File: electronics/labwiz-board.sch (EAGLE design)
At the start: 91 parts, among them J1 SD_MICRO_SDIO_1BIT, J2 CORTEX_DEBUGSMD, J3 DNP, U1 STM32F10XRXT6, U2 MCP73831, U4 MIC5219-3.3V, X2 M12_BOTTOM_CONTACTS_FPC_1MM, Y3 32.768kHz

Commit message: Updated .gitignore. Comitting unknown schematic updates.
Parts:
- removed J4: (no value), SparkFun-Connectors:M03PTH
- added TP10, TP8, TP9: DNP, PaxInstruments-Connectors:M01_PAD_1MM
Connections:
- net GND: now also TP10.P$1; no longer J4.3
- net USART1_RX: now also TP9.P$1; no longer J4.2
- net USART1_TX: now also TP8.P$1; no longer J4.1
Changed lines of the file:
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@@
 <part name="C16" library="PaxInstruments-RCL" deviceset="CAPACITOR_FIXED" device="_0402" technology="_100NF" value="100nF"/>
 <part name="TP7" library="PaxInstruments-Connectors" deviceset="M01" device="_PAD_1MM" value="DNP"/>
-<part name="J4" library="SparkFun-Connectors" deviceset="M03" device="PTH"/>
 <part name="GND21" library="PaxInstruments-Aesthetics" deviceset="GND" device="" value="GND"/>
+<part name="TP8" library="PaxInstruments-Connectors" deviceset="M01" device="_PAD_1MM" value="DNP"/>
+<part name="TP9" library="PaxInstruments-Connectors" deviceset="M01" device="_PAD_1MM" value="DNP"/>
+<part name="TP10" library="PaxInstruments-Connectors" deviceset="M01" device="_PAD_1MM" value="DNP"/>
 </parts>
 <sheets>
@@
 <instance part="C16" gate="G$1" x="165.1" y="63.5" rot="MR180"/>
 <instance part="TP7" gate="G$1" x="299.72" y="119.38" rot="R180"/>
-<instance part="J4" gate="J$1" x="281.94" y="121.92" rot="R180"/>
 <instance part="GND21" gate="G$1" x="271.78" y="116.84"/>
+<instance part="TP8" gate="G$1" x="276.86" y="124.46"/>
+<instance part="TP9" gate="G$1" x="276.86" y="121.92"/>
+<instance part="TP10" gate="G$1" x="276.86" y="119.38"/>
 </instances>
 <busses>
@@
 </segment>
 <segment>
-<pinref part="J4" gate="J$1" pin="3"/>
 <pinref part="GND21" gate="G$1" pin="GND"/>
 <wire x1="274.32" y1="119.38" x2="271.78" y2="119.38" width="0.1524" layer="91"/>
 <wire x1="271.78" y1="119.38" x2="271.78" y2="116.84" width="0.1524" layer="91"/>
+<pinref part="TP10" gate="G$1" pin="P$1"/>
 </segment>
 </net>
@@
 <segment>
 <label x="259.08" y="124.46" size="1.27" layer="95" rot="R180" xref="yes"/>
-<pinref part="J4" gate="J$1" pin="1"/>
 <wire x1="259.08" y1="124.46" x2="274.32" y2="124.46" width="0.1524" layer="91"/>
+<pinref part="TP8" gate="G$1" pin="P$1"/>
 </segment>
 <segment>
@@
 <segment>
 <label x="259.08" y="121.92" size="1.27" layer="95" rot="R180" xref="yes"/>
-<pinref part="J4" gate="J$1" pin="2"/>
 <wire x1="259.08" y1="121.92" x2="274.32" y2="121.92" width="0.1524" layer="91"/>
-</segment>
-<segment>
+<pinref part="TP9" gate="G$1" pin="P$1"/>
+</segment>
+<segment>

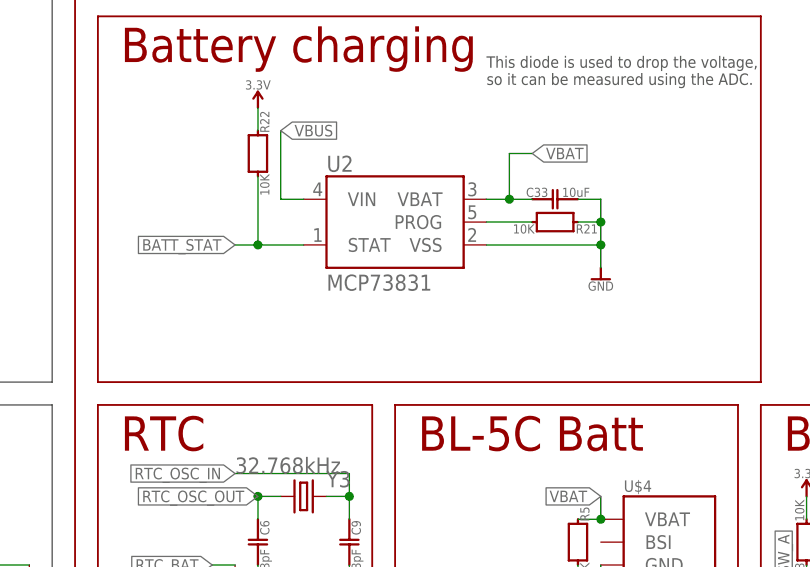
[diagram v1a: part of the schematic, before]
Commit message: Updated MCP73831/2 name.
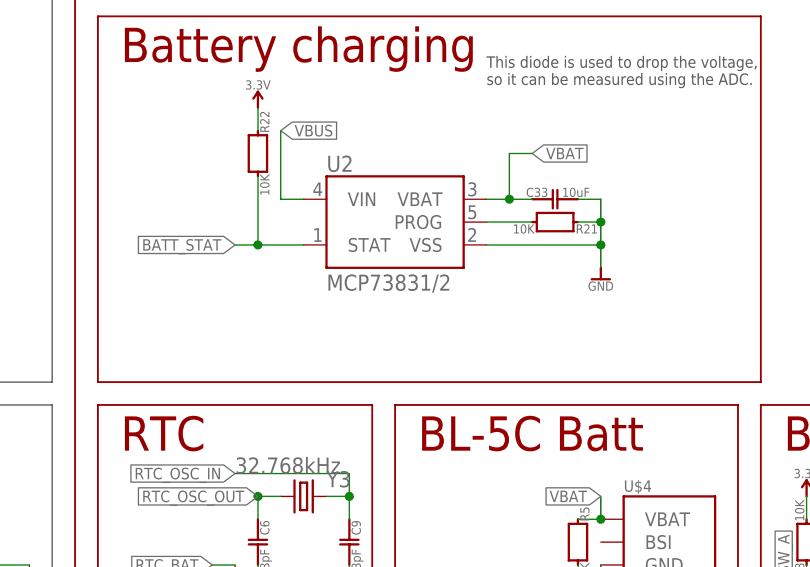
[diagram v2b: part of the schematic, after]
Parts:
- U2: value MCP73831 -> MCP73831/2; device PaxInstruments-PowerIC:MCP73831 -> PaxInstruments-PowerIC:MCP73831/2
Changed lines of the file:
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@@
 <part name="C32" library="PaxInstruments-RCL" deviceset="CAPACITOR_FIXED" device="_0402" technology="_100NF" value="100nF"/>
 <part name="U$9" library="PaxInstruments-FreqCtrl" deviceset="NX3225GD" device="" value="8MHz"/>
-<part name="U2" library="PaxInstruments-PowerIC" deviceset="MCP73831" device=""/>
+<part name="U2" library="PaxInstruments-PowerIC" deviceset="MCP73831/2" device=""/>
 <part name="GND45" library="PaxInstruments-Aesthetics" deviceset="GND" device=""/>
 <part name="R21" library="PaxInstruments-RCL" deviceset="RESISTOR_FIXED" device="_0402" technology="_10K" value="10K">

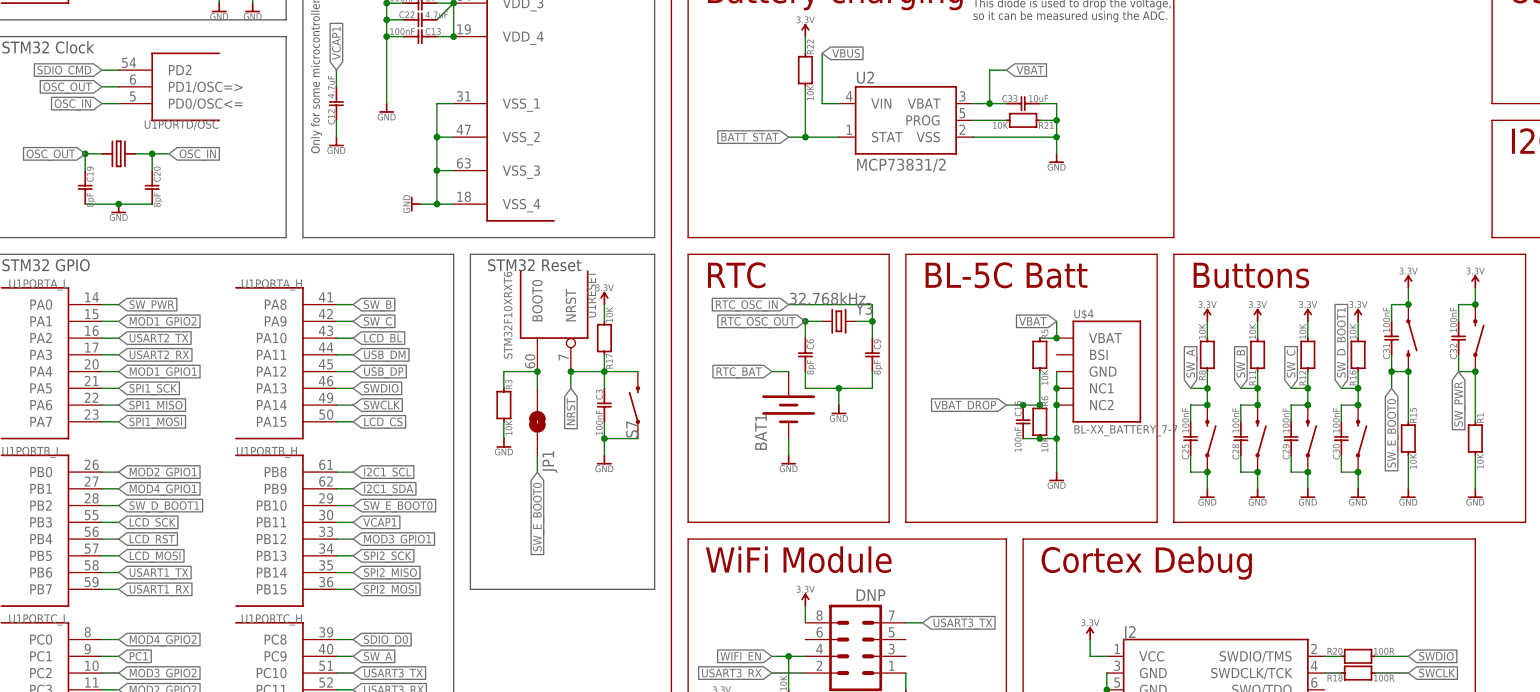
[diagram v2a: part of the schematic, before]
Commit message: Swapped the net names for SW_D and SW_E. The physical locations were swapped on the v0.3 board.
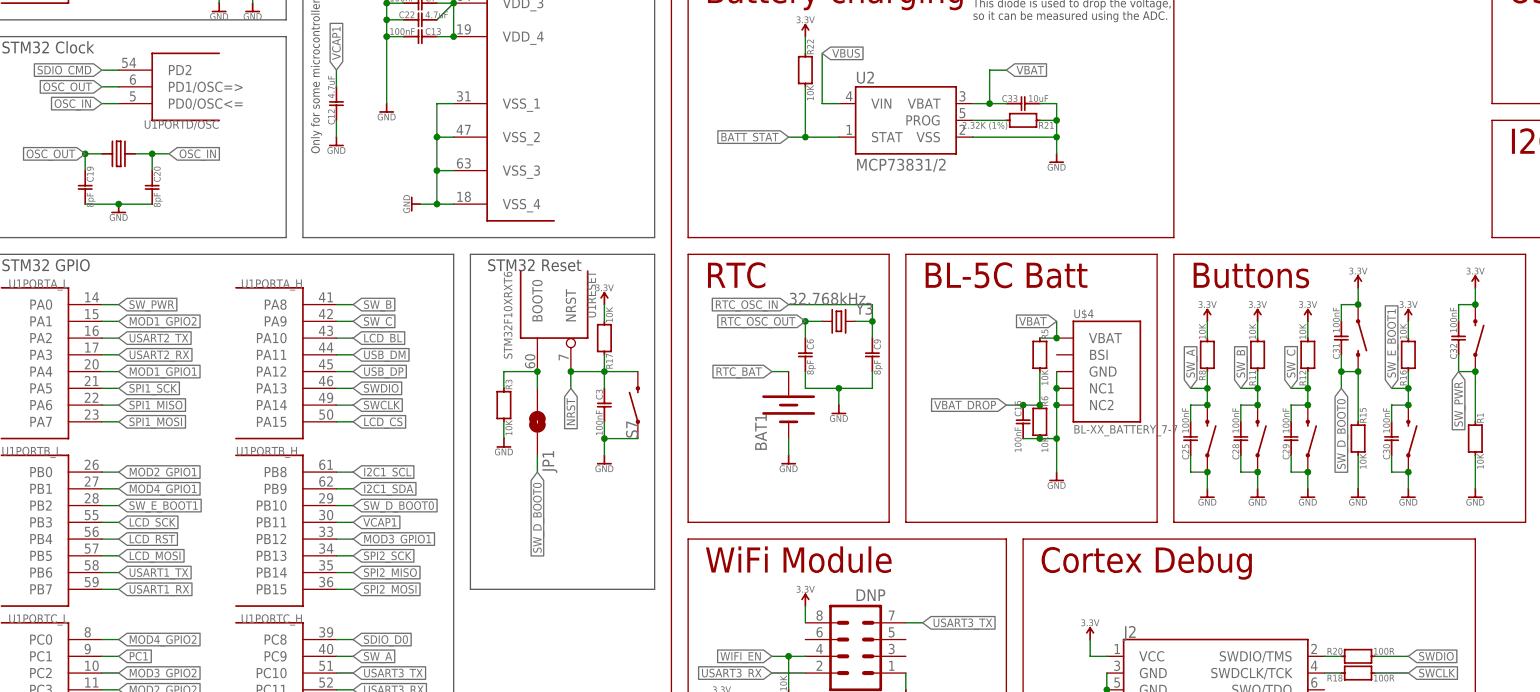
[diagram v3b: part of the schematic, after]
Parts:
- R21: value 10K -> 2.32K (1%); device PaxInstruments-RCL:RESISTOR_FIXED_10K_0402 -> PaxInstruments-RCL:RESISTOR_FIXED_2.32K_0402
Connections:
- net SW_D_BOOT1 renamed SW_E_BOOT1
- net SW_E_BOOT0 renamed SW_D_BOOT0
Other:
- moved on the sheet: C30, C31, R15, R16
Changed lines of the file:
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@@
 <part name="U2" library="PaxInstruments-PowerIC" deviceset="MCP73831/2" device=""/>
 <part name="GND45" library="PaxInstruments-Aesthetics" deviceset="GND" device=""/>
-<part name="R21" library="PaxInstruments-RCL" deviceset="RESISTOR_FIXED" device="_0402" technology="_10K" value="10K">
+<part name="R21" library="PaxInstruments-RCL" deviceset="RESISTOR_FIXED" device="_0402" technology="_2.32K" value="2.32K (1%)">
 <attribute name="MPN" value=""/>
 <attribute name="POPULATE" value=""/>
@@
 <attribute name="POPULATE" x="208.28" y="73.66" size="1.778" layer="96" display="off"/>
 </instance>
-<instance part="R15" gate="G$1" x="223.52" y="60.96" rot="R180">
-<attribute name="MPN" x="223.52" y="60.96" size="1.778" layer="96" rot="R180" display="off"/>
-<attribute name="POPULATE" x="223.52" y="60.96" size="1.778" layer="96" rot="R180" display="off"/>
-</instance>
-<instance part="R16" gate="G$1" x="215.9" y="73.66">
-<attribute name="MPN" x="215.9" y="73.66" size="1.778" layer="96" display="off"/>
-<attribute name="POPULATE" x="215.9" y="73.66" size="1.778" layer="96" display="off"/>
+<instance part="R15" gate="G$1" x="215.9" y="60.96" rot="R180">
+<attribute name="MPN" x="215.9" y="60.96" size="1.778" layer="96" rot="R180" display="off"/>
+<attribute name="POPULATE" x="215.9" y="60.96" size="1.778" layer="96" rot="R180" display="off"/>
+</instance>
+<instance part="R16" gate="G$1" x="223.52" y="73.66">
+<attribute name="MPN" x="223.52" y="73.66" size="1.778" layer="96" display="off"/>
+<attribute name="POPULATE" x="223.52" y="73.66" size="1.778" layer="96" display="off"/>
 </instance>
 <instance part="C26" gate="G$1" x="106.68" y="170.18">
@@
 </instance>
 <instance part="GND6" gate="G$1" x="208.28" y="53.34"/>
-<instance part="S4" gate="G$1" x="223.52" y="76.2" smashed="yes" rot="R270">
-<attribute name="MF" x="223.52" y="76.2" size="1.778" layer="96" rot="R270" display="off"/>
-<attribute name="MPN" x="223.52" y="76.2" size="1.778" layer="96" rot="R270" display="off"/>
-</instance>
-<instance part="S5" gate="G$1" x="215.9" y="60.96" smashed="yes" rot="MR90">
-<attribute name="MF" x="215.9" y="60.96" size="1.778" layer="96" rot="MR90" display="off"/>
-<attribute name="MPN" x="215.9" y="60.96" size="1.778" layer="96" rot="MR90" display="off"/>
+<instance part="S4" gate="G$1" x="215.9" y="76.2" smashed="yes" rot="R270">
+<attribute name="MF" x="215.9" y="76.2" size="1.778" layer="96" rot="R270" display="off"/>
+<attribute name="MPN" x="215.9" y="76.2" size="1.778" layer="96" rot="R270" display="off"/>
+</instance>
+<instance part="S5" gate="G$1" x="223.52" y="60.96" smashed="yes" rot="MR90">
+<attribute name="MF" x="223.52" y="60.96" size="1.778" layer="96" rot="MR90" display="off"/>
+<attribute name="MPN" x="223.52" y="60.96" size="1.778" layer="96" rot="MR90" display="off"/>
 </instance>
 <instance part="R19" gate="G$1" x="266.7" y="55.88" rot="R270">
@@
 </instance>
 <instance part="P+6" gate="G$1" x="233.68" y="83.82" rot="MR0"/>
-<instance part="P+7" gate="G$1" x="215.9" y="78.74" rot="MR0"/>
-<instance part="P+8" gate="G$1" x="223.52" y="83.82" rot="MR0"/>
+<instance part="P+7" gate="G$1" x="223.52" y="78.74" rot="MR0"/>
+<instance part="P+8" gate="G$1" x="215.9" y="83.82" rot="MR0"/>
 <instance part="P+10" gate="G$1" x="193.04" y="78.74" rot="MR0"/>
 <instance part="P+11" gate="G$1" x="200.66" y="78.74" rot="MR0"/>
 <instance part="P+12" gate="G$1" x="208.28" y="78.74" rot="MR0"/>
 <instance part="GND31" gate="G$1" x="233.68" y="53.34"/>
-<instance part="GND33" gate="G$1" x="215.9" y="53.34"/>
+<instance part="GND33" gate="G$1" x="223.52" y="53.34"/>
 <instance part="GND42" gate="G$1" x="200.66" y="53.34"/>
-<instance part="GND43" gate="G$1" x="223.52" y="53.34"/>
+<instance part="GND43" gate="G$1" x="215.9" y="53.34"/>
 <instance part="GND44" gate="G$1" x="193.04" y="53.34"/>
 <instance part="C25" gate="G$1" x="190.5" y="60.96"/>
 <instance part="C28" gate="G$1" x="198.12" y="60.96"/>
 <instance part="C29" gate="G$1" x="205.74" y="60.96"/>
-<instance part="C30" gate="G$1" x="213.36" y="60.96"/>
-<instance part="C31" gate="G$1" x="220.98" y="76.2"/>
+<instance part="C30" gate="G$1" x="220.98" y="60.96"/>
+<instance part="C31" gate="G$1" x="213.36" y="76.2"/>
 <instance part="C32" gate="G$1" x="231.14" y="76.2"/>
 <instance part="U$9" gate="G$1" x="27.94" y="104.14" smashed="yes"/>
@@
 <pinref part="P+7" gate="G$1" pin="3.3V"/>
 <pinref part="R16" gate="G$1" pin="1"/>
-<wire x1="215.9" y1="76.2" x2="215.9" y2="78.74" width="0.1524" layer="91"/>
+<wire x1="223.52" y1="76.2" x2="223.52" y2="78.74" width="0.1524" layer="91"/>
 </segment>
 <segment>
 <pinref part="S4" gate="G$1" pin="1"/>
 <pinref part="P+8" gate="G$1" pin="3.3V"/>
-<wire x1="223.52" y1="81.28" x2="223.52" y2="83.82" width="0.1524" layer="91"/>
+<wire x1="215.9" y1="81.28" x2="215.9" y2="83.82" width="0.1524" layer="91"/>
 <pinref part="C31" gate="G$1" pin="2"/>
-<wire x1="220.98" y1="78.74" x2="220.98" y2="81.28" width="0.1524" layer="91"/>
-<wire x1="220.98" y1="81.28" x2="223.52" y2="81.28" width="0.1524" layer="91"/>
-<junction x="223.52" y="81.28"/>
+<wire x1="213.36" y1="78.74" x2="213.36" y2="81.28" width="0.1524" layer="91"/>
+<wire x1="213.36" y1="81.28" x2="215.9" y2="81.28" width="0.1524" layer="91"/>
+<junction x="215.9" y="81.28"/>
 </segment>
 <segment>
@@
 <pinref part="S5" gate="G$1" pin="1"/>
 <pinref part="GND33" gate="G$1" pin="GND"/>
-<wire x1="215.9" y1="53.34" x2="215.9" y2="55.88" width="0.1524" layer="91"/>
+<wire x1="223.52" y1="53.34" x2="223.52" y2="55.88" width="0.1524" layer="91"/>
 <pinref part="C30" gate="G$1" pin="1"/>
-<wire x1="215.9" y1="55.88" x2="213.36" y2="55.88" width="0.1524" layer="91"/>
-<wire x1="213.36" y1="55.88" x2="213.36" y2="58.42" width="0.1524" layer="91"/>
-<junction x="215.9" y="55.88"/>
+<wire x1="223.52" y1="55.88" x2="220.98" y2="55.88" width="0.1524" layer="91"/>
+<wire x1="220.98" y1="55.88" x2="220.98" y2="58.42" width="0.1524" layer="91"/>
+<junction x="223.52" y="55.88"/>
 </segment>
 <segment>
@@
 <pinref part="R15" gate="G$1" pin="1"/>
 <pinref part="GND43" gate="G$1" pin="GND"/>
-<wire x1="223.52" y1="58.42" x2="223.52" y2="53.34" width="0.1524" layer="91"/>
+<wire x1="215.9" y1="58.42" x2="215.9" y2="53.34" width="0.1524" layer="91"/>
 </segment>
 <segment>
@@
 </segment>
 </net>
-<net name="SW_E_BOOT0" class="0">
+<net name="SW_D_BOOT0" class="0">
 <segment>
 <label x="91.44" y="55.88" size="1.27" layer="95" rot="R270" xref="yes"/>
@@
 <pinref part="R15" gate="G$1" pin="2"/>
 <pinref part="S4" gate="G$1" pin="2"/>
-<wire x1="223.52" y1="71.12" x2="223.52" y2="63.5" width="0.1524" layer="91"/>
-<label x="220.98" y="68.58" size="1.27" layer="95" rot="R270" xref="yes"/>
-<junction x="223.52" y="71.12"/>
+<wire x1="215.9" y1="71.12" x2="215.9" y2="63.5" width="0.1524" layer="91"/>
+<label x="213.36" y="68.58" size="1.27" layer="95" rot="R270" xref="yes"/>
+<junction x="215.9" y="71.12"/>
 <pinref part="C31" gate="G$1" pin="1"/>
-<wire x1="220.98" y1="68.58" x2="220.98" y2="71.12" width="0.1524" layer="91"/>
-<wire x1="220.98" y1="71.12" x2="220.98" y2="73.66" width="0.1524" layer="91"/>
-<wire x1="223.52" y1="71.12" x2="220.98" y2="71.12" width="0.1524" layer="91"/>
-<junction x="220.98" y="71.12"/>
+<wire x1="213.36" y1="68.58" x2="213.36" y2="71.12" width="0.1524" layer="91"/>
+<wire x1="213.36" y1="71.12" x2="213.36" y2="73.66" width="0.1524" layer="91"/>
+<wire x1="215.9" y1="71.12" x2="213.36" y2="71.12" width="0.1524" layer="91"/>
+<junction x="213.36" y="71.12"/>
 </segment>
 </net>
@@
 </segment>
 </net>
-<net name="SW_D_BOOT1" class="0">
+<net name="SW_E_BOOT1" class="0">
 <segment>
 <pinref part="U1" gate="PORTB_L" pin="PB2"/>
@@
 <pinref part="R16" gate="G$1" pin="2"/>
 <pinref part="S5" gate="G$1" pin="2"/>
-<wire x1="215.9" y1="66.04" x2="215.9" y2="68.58" width="0.1524" layer="91"/>
-<wire x1="215.9" y1="68.58" x2="215.9" y2="71.12" width="0.1524" layer="91"/>
-<label x="213.36" y="68.58" size="1.27" layer="95" rot="R90" xref="yes"/>
-<wire x1="213.36" y1="68.58" x2="215.9" y2="68.58" width="0.1524" layer="91"/>
-<junction x="215.9" y="68.58"/>
+<wire x1="223.52" y1="66.04" x2="223.52" y2="68.58" width="0.1524" layer="91"/>
+<wire x1="223.52" y1="68.58" x2="223.52" y2="71.12" width="0.1524" layer="91"/>
+<label x="220.98" y="68.58" size="1.27" layer="95" rot="R90" xref="yes"/>
+<wire x1="220.98" y1="68.58" x2="223.52" y2="68.58" width="0.1524" layer="91"/>
+<junction x="223.52" y="68.58"/>
 <pinref part="C30" gate="G$1" pin="2"/>
-<wire x1="215.9" y1="66.04" x2="213.36" y2="66.04" width="0.1524" layer="91"/>
-<wire x1="213.36" y1="66.04" x2="213.36" y2="63.5" width="0.1524" layer="91"/>
-<junction x="215.9" y="66.04"/>
-</segment>
-</net>
+<wire x1="223.52" y1="66.04" x2="220.98" y2="66.04" width="0.1524" layer="91"/>
+<wire x1="220.98" y1="66.04" x2="220.98" y2="63.5" width="0.1524" layer="91"/>
+<junction x="223.52" y="66.04"/>
+</segment>
+</net>

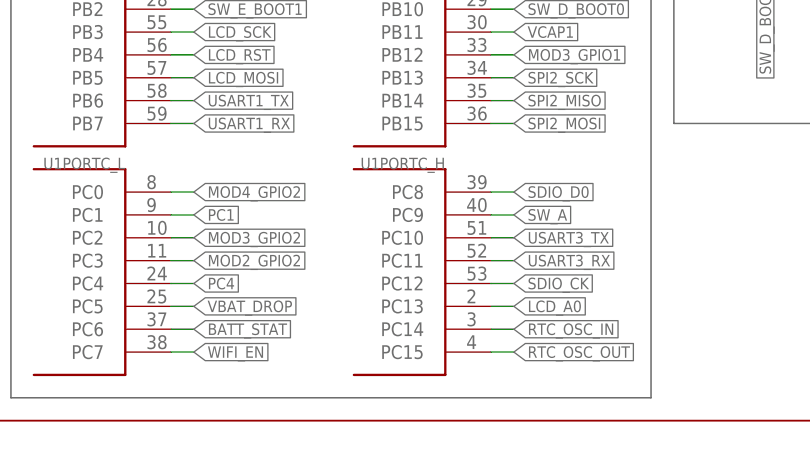
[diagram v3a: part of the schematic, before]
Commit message: Swapped WIFI_EN with SW_A to avoid interrupt sharing.
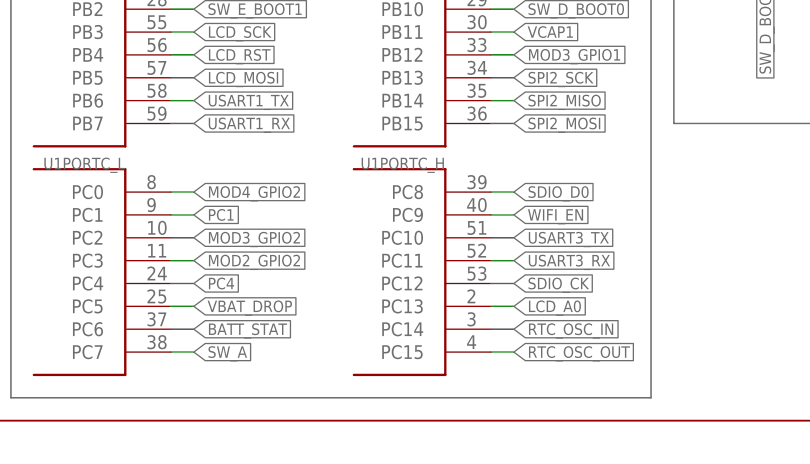
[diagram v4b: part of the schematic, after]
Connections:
- net SW_A: now also U1PORTC_L.PC7; no longer U1PORTC_H.PC9
- net WIFI_EN: now also U1PORTC_H.PC9; no longer U1PORTC_L.PC7
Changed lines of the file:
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@@
 </segment>
 <segment>
-<pinref part="U1" gate="PORTC_H" pin="PC9"/>
-<wire x1="60.96" y1="27.94" x2="63.5" y2="27.94" width="0.1524" layer="91"/>
-<label x="63.5" y="27.94" size="1.27" layer="95" xref="yes"/>
+<pinref part="U1" gate="PORTC_L" pin="PC7"/>
+<wire x1="25.4" y1="12.7" x2="27.94" y2="12.7" width="0.1524" layer="91"/>
+<label x="27.94" y="12.7" size="1.27" layer="95" xref="yes"/>
 </segment>
 </net>
@@
 </segment>
 <segment>
-<pinref part="U1" gate="PORTC_L" pin="PC7"/>
-<wire x1="25.4" y1="12.7" x2="27.94" y2="12.7" width="0.1524" layer="91"/>
-<label x="27.94" y="12.7" size="1.27" layer="95" xref="yes"/>
-</segment>
-</net>
+<pinref part="U1" gate="PORTC_H" pin="PC9"/>
+<wire x1="60.96" y1="27.94" x2="63.5" y2="27.94" width="0.1524" layer="91"/>
+<label x="63.5" y="27.94" size="1.27" layer="95" xref="yes"/>
+</segment>
+</net>
